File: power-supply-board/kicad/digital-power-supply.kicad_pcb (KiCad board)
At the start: 2 copper layers, 106.5 x 115 mm, 18 parts, among them J1 5V, J2 5V, J3 +12V, J4 +12V, J5 -12V, J6 -12V, SW1 SW

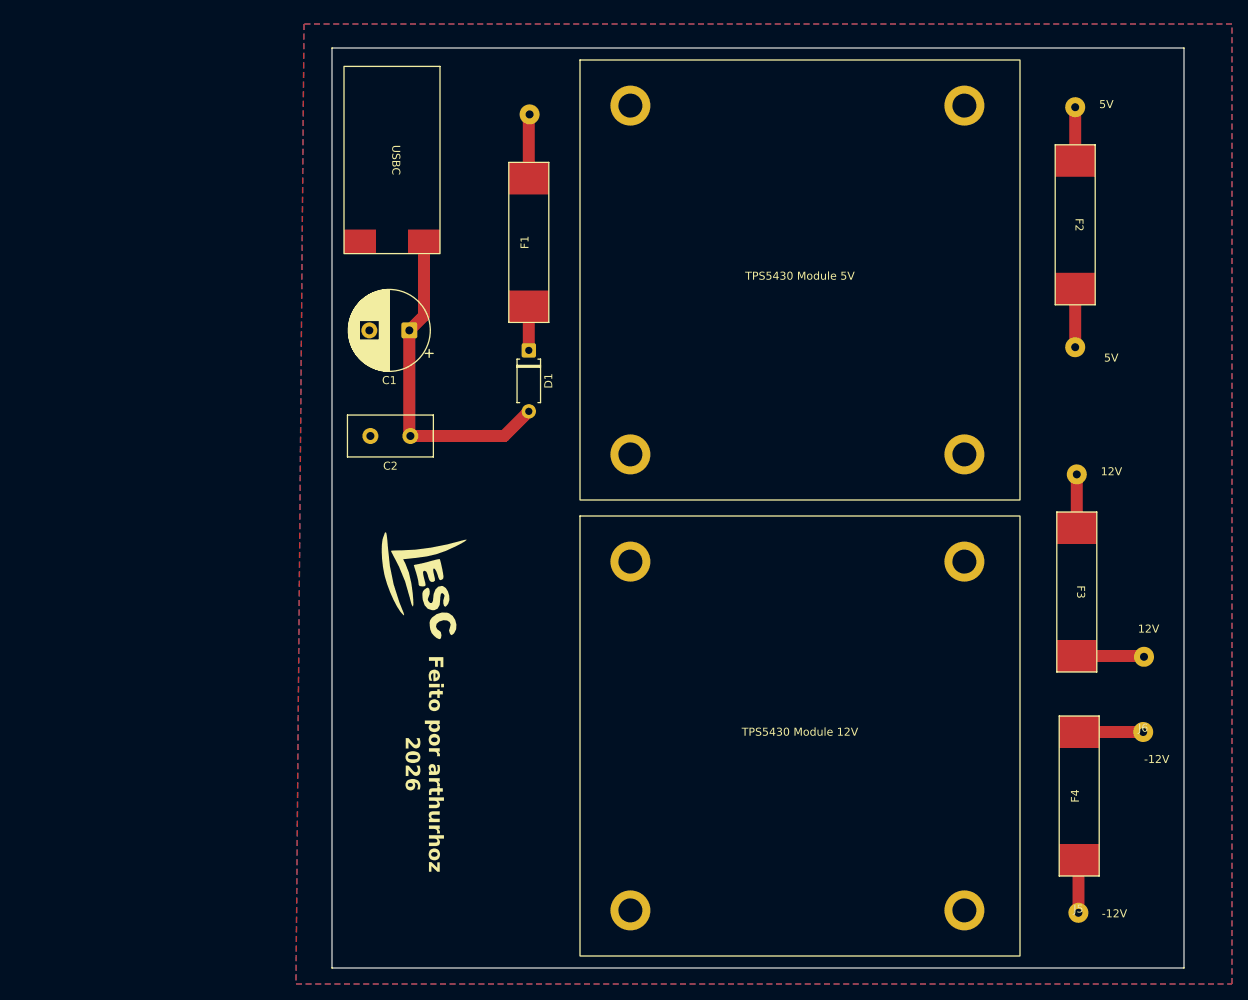
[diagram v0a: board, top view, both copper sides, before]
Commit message: feat: new pcb design with crowbar overvoltage protection
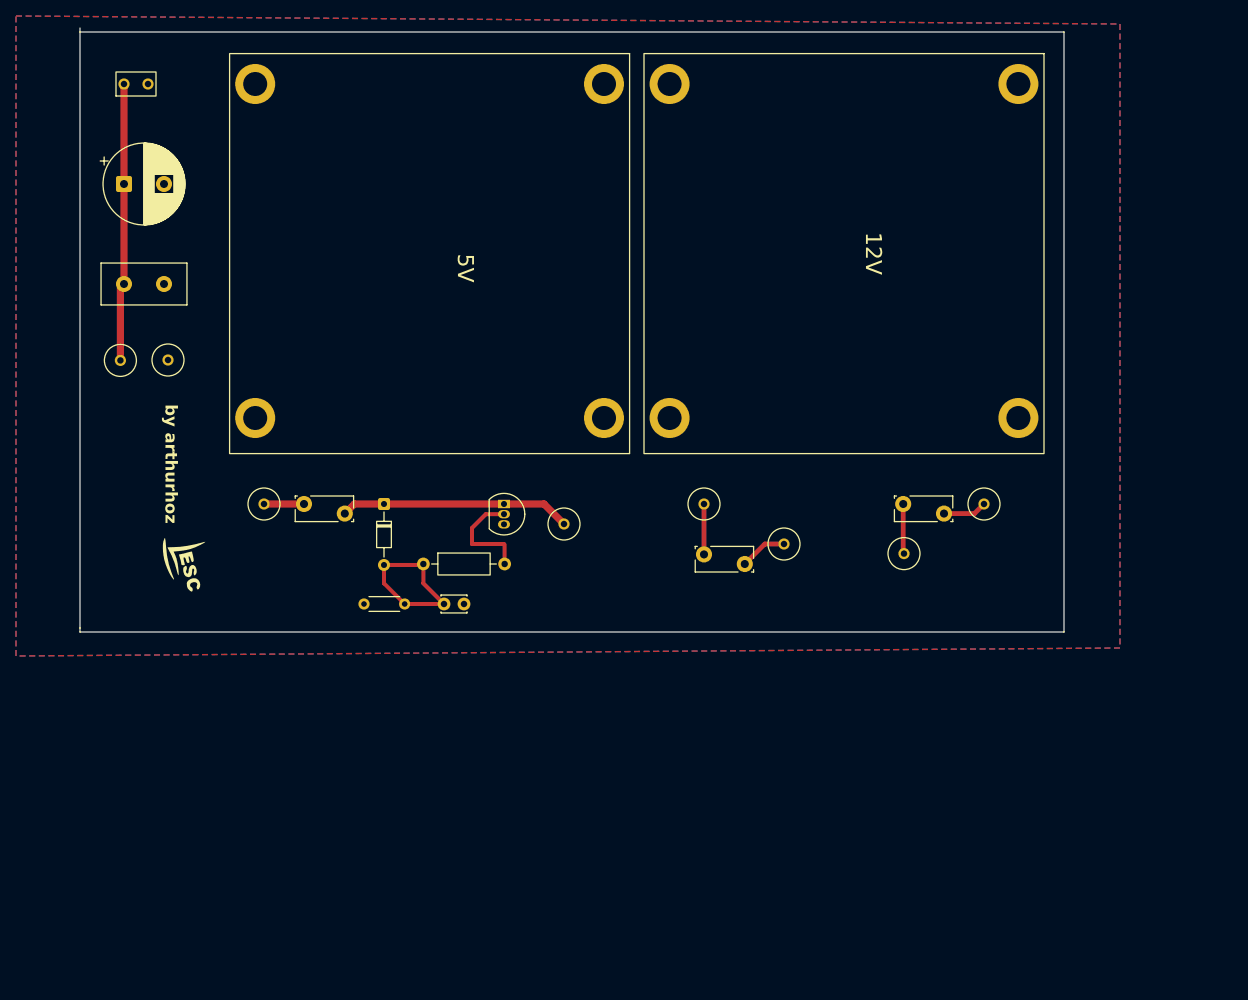
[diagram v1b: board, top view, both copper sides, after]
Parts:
- removed F4: Fuse, footprint:Fuse5x20mm
- removed SW1: SW, footprint:SW
- removed TPS5430 Module 12V: TPS5430 Module 12V, footprint:TPS5430_Module
- removed TPS5430 Module 5V: TPS5430 Module 5V, footprint:TPS5430_Module
- removed USBC: USBC Module, footprint:USBC_Module
- added C4: 1nF, Capacitor_THT:C_Disc_D3.0mm_W2.0mm_P2.50mm, F.Cu at (137.5, 87.5)
- added J7: GND, footprints:Connector, F.Cu at (103.0, 57.0)
- added J8: Conn_01x01_Socket, footprints:Connector, F.Cu at (97.0, 57.0)
- added Q1: BT151-500R, Package_TO_SOT_THT:TO-92_Inline, F.Cu at (145.0, 75.0)
- added R1: 4k7 1/8W, Resistor_THT:R_Axial_DIN0204_L3.6mm_D1.6mm_P5.08mm_Horizontal, F.Cu at (127.5, 87.5)
- added R2: 330 1/4W, Resistor_THT:R_Axial_DIN0207_L6.3mm_D2.5mm_P10.16mm_Horizontal, F.Cu at (134.9, 82.5)
- added U1: USBC Module, footprints:USBC_Module, F.Cu at (99.0, 22.5)
- added U2: TPS5430 Module 5V, footprints:TPS5430_Module, F.Cu at (135.7, 43.7)
- added U3: TPS5430 Module 12V, footprints:TPS5430_Module, F.Cu at (187.5, 43.7)
- D1: value D -> 1N4734A; footprint Diode_THT:D_A-405_P7.62mm_Horizontal -> Diode_THT:D_DO-34_SOD68_P7.62mm_Horizontal
- F1: value Fuse -> RXEF200 2A; footprint footprint:Fuse5x20mm -> Fuse:Fuse_Bourns_MF-RG300
- F2, F3: value Fuse -> RXEF110 1A1; footprint footprint:Fuse5x20mm -> Fuse:Fuse_Bourns_MF-RG300
- J1, J2, J3, J4, J5, J6: footprint footprint:SW -> footprints:Connector
- moved J1 112.9 mm to (115.0, 75.0)
- moved J2 67.6 mm to (152.5, 77.5)
- moved F2 62.1 mm to (170.0, 81.3), turned to 0 degrees
- moved J5 52.4 mm to (205.0, 75.0)
- moved J4 47.2 mm to (180.0, 80.0)
- moved J3 46.7 mm to (170.0, 75.0)
- moved F1 43.1 mm to (120.0, 75.0), turned to 0 degrees
- moved C2 40.5 mm to (97.5, 47.5), turned to 0 degrees
- moved C1 40.1 mm to (97.5, 35.0), turned to 0 degrees
- moved J6 37.3 mm to (195.0, 81.2)
- moved G*** 30.1 mm to (105.0, 82.5)
- moved D1 26.4 mm to (130.0, 75.0)
- moved F3 19.3 mm to (200.0, 76.2), turned to 180 degrees
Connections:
- C1 pad 1: Net-(D1-A) -> /VIN
- C2 pad 1: Net-(D1-A) -> /VIN
- D1 pad 1: Net-(D1-K) -> /5V
- F1 pad 1: Net-(D1-K) -> Net-(J1-Pin_1)
- F1 pad 2: Net-(SW1-B) -> /5V
- F2 pad 1: Net-(J1-Pin_1) -> Net-(J3-Pin_1)
- F2 pad 2: /5V -> /+12V
- F3 pad 1: Net-(J3-Pin_1) -> Net-(J5-Pin_1)
- F3 pad 2: /+12V -> /-12V
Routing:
- net /VIN: track 8.04 -> 34.7 mm
- net /5V: track 7.30 -> 28.9 mm
- net Net-(D1-A): track 41.2 -> 21.9 mm
- net Net-(Q1-G): track 0.00 -> 13.2 mm
- net /-12V: track 14.6 -> 6.24 mm
- net Net-(D1-K): track 5.50 -> 0.00 mm
- net Net-(J5-Pin_1): track 0.00 -> 5.50 mm
- net /+12V: track 8.44 -> 5.94 mm
- net Net-(J1-Pin_1): track 6.70 -> 5.00 mm
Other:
- board size 106.5 x 115 mm -> 123 x 75.5 mm
- board text added: "by arthurhoz"
- board text removed: "-12V"
- board text removed: "Feito por arthurhoz 2026"

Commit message: docs & fix: create schematics and pcb images and remove copper fill in tps modules zones
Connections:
- U1 pad 1: /VIN -> Net-(SW1-B)
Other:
- board size 123 x 75.5 mm -> 125 x 72.5 mm
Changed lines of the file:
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@@
 			(layers "*.Cu" "*.Mask")
 			(remove_unused_layers no)
-			(net "/VIN")
+			(net "Net-(SW1-B)")
 			(pinfunction "VIN_1")
 			(pintype "power_out")
@@
 	)
 	(gr_line
-		(start 92 90.5)
-		(end 92 15.5)
+		(start 88.5 17.5)
+		(end 213.5 17.5)
 		(stroke
 			(width 0.05)
@@
 	)
 	(gr_line
-		(start 92 90.5)
-		(end 92 91)
+		(start 88.5 90)
+		(end 88.5 17.5)
+		(stroke
+			(width 0.05)
+			(type solid)
+		)
+		(layer "Edge.Cuts")
+	)
+	(gr_line
+		(start 213.5 17.5)
+		(end 213.5 90)
 		(stroke
 			(width 0.05)
@@
 	)
 	(gr_line
-		(start 92 91)
-		(end 215 91)
-		(stroke
-			(width 0.05)
-			(type default)
-		)
-		(layer "Edge.Cuts")
-	)
-	(gr_line
-		(start 215 16)
-		(end 91.998984 16)
-		(stroke
-			(width 0.05)
-			(type solid)
-		)
-		(layer "Edge.Cuts")
-	)
-	(gr_line
-		(start 215 16)
-		(end 215 91)
+		(start 213.5 90)
+		(end 88.5 90)
 		(stroke
 			(width 0.05)
@@
 	)
 	(segment
+		(start 97.05 57.05)
+		(end 97.05 47.95)
+		(width 0.9)
+		(layer "F.Cu")
+		(net "/VIN")
+	)
+	(segment
+		(start 97.5 22.5)
+		(end 97.5 35)
+		(width 0.9)
+		(layer "F.Cu")
+		(net "/VIN")
+	)
+	(segment
+		(start 97.5 35)
+		(end 97.5 47.5)
+		(width 0.9)
+		(layer "F.Cu")
+		(net "/VIN")
+	)
+	(segment
+		(start 97.05 47.95)
+		(end 97.5 47.5)
+		(width 0.2)
+		(layer "F.Cu")
+		(net "/VIN")
+	)
+	(segment
+		(start 194.9 81.1)
+		(end 195 81.2)
+		(width 0.2)
+		(layer "F.Cu")
+		(net "/-12V")
+	)
+	(segment
+		(start 194.9 75)
+		(end 194.9 81.1)
+		(width 0.6)
+		(layer "F.Cu")
+		(net "/-12V")
+	)
+	(segment
+		(start 205 75)
+		(end 203.8 76.2)
+		(width 0.6)
+		(layer "F.Cu")
+		(net "Net-(J5-Pin_1)")
+	)
+	(segment
+		(start 203.8 76.2)
+		(end 200 76.2)
+		(width 0.6)
+		(layer "F.Cu")
+		(net "Net-(J5-Pin_1)")
+	)
+	(segment
+		(start 170 75)
+		(end 170 81.3)
+		(width 0.6)
+		(layer "F.Cu")
+		(net "Net-(J3-Pin_1)")
+	)
+	(segment
+		(start 175.1 82.5)
+		(end 177.6 80)
+		(width 0.6)
+		(layer "F.Cu")
+		(net "/+12V")
+	)
+	(segment
+		(start 177.6 80)
+		(end 180 80)
+		(width 0.6)
+		(layer "F.Cu")
+		(net "/+12V")
+	)
+	(segment
+		(start 130 75)
+		(end 145 75)
+		(width 0.9)
+		(layer "F.Cu")
+		(net "/5V")
+	)
+	(segment
+		(start 145 75)
+		(end 150 75)
+		(width 0.9)
+		(layer "F.Cu")
+		(net "/5V")
+	)
+	(segment
+		(start 126.3 75)
+		(end 130 75)
+		(width 0.9)
+		(layer "F.Cu")
+		(net "/5V")
+	)
+	(segment
+		(start 125.1 76.2)
+		(end 126.3 75)
+		(width 0.9)
+		(layer "F.Cu")
+		(net "/5V")
+	)
+	(segment
+		(start 150 75)
+		(end 152.5 77.5)
+		(width 0.9)
+		(layer "F.Cu")
+		(net "/5V")
+	)
+	(segment
+		(start 141 78)
+		(end 142.73 76.27)
+		(width 0.5)
+		(layer "F.Cu")
+		(net "Net-(Q1-G)")
+	)
+	(segment
+		(start 145.08 82.5)
+		(end 145.08 80.08)
+		(width 0.5)
+		(layer "F.Cu")
+		(net "Net-(Q1-G)")
+	)
+	(segment
+		(start 145.08 80.08)
+		(end 145 80)
+		(width 0.2)
+		(layer "F.Cu")
+		(net "Net-(Q1-G)")
+	)
+	(segment
+		(start 141 80)
+		(end 141 78)
+		(width 0.5)
+		(layer "F.Cu")
+		(net "Net-(Q1-G)")
+	)
+	(segment
+		(start 142.73 76.27)
+		(end 145 76.27)
+		(width 0.5)
+		(layer "F.Cu")
+		(net "Net-(Q1-G)")
+	)
+	(segment
+		(start 145 80)
+		(end 141 80)
+		(width 0.5)
+		(layer "F.Cu")
+		(net "Net-(Q1-G)")
+	)
+	(segment
 		(start 115 75)
 		(end 120 75)
@@
 	)
 	(segment
-		(start 130 75)
-		(end 145 75)
-		(width 0.9)
-		(layer "F.Cu")
-		(net "/5V")
-	)
-	(segment
-		(start 145 75)
-		(end 150 75)
-		(width 0.9)
-		(layer "F.Cu")
-		(net "/5V")
-	)
-	(segment
-		(start 126.3 75)
-		(end 130 75)
-		(width 0.9)
-		(layer "F.Cu")
-		(net "/5V")
-	)
-	(segment
-		(start 125.1 76.2)
-		(end 126.3 75)
-		(width 0.9)
-		(layer "F.Cu")
-		(net "/5V")
-	)
-	(segment
-		(start 150 75)
-		(end 152.5 77.5)
-		(width 0.9)
-		(layer "F.Cu")
-		(net "/5V")
-	)
-	(segment
-		(start 205 75)
-		(end 203.8 76.2)
-		(width 0.6)
-		(layer "F.Cu")
-		(net "Net-(J5-Pin_1)")
-	)
-	(segment
-		(start 203.8 76.2)
-		(end 200 76.2)
-		(width 0.6)
-		(layer "F.Cu")
-		(net "Net-(J5-Pin_1)")
-	)
-	(segment
 		(start 132.58 87.5)
 		(end 137.5 87.5)
@@
 		(net "Net-(D1-A)")
 	)
-	(segment
-		(start 194.9 81.1)
-		(end 195 81.2)
-		(width 0.2)
-		(layer "F.Cu")
-		(net "/-12V")
-	)
-	(segment
-		(start 194.9 75)
-		(end 194.9 81.1)
-		(width 0.6)
-		(layer "F.Cu")
-		(net "/-12V")
-	)
-	(segment
-		(start 97.05 57.05)
-		(end 97.05 47.95)
-		(width 0.9)
-		(layer "F.Cu")
-		(net "/VIN")
-	)
-	(segment
-		(start 97.5 22.5)
-		(end 97.5 35)
-		(width 0.9)
-		(layer "F.Cu")
-		(net "/VIN")
-	)
-	(segment
-		(start 97.5 35)
-		(end 97.5 47.5)
-		(width 0.9)
-		(layer "F.Cu")
-		(net "/VIN")
-	)
-	(segment
-		(start 97.05 47.95)
-		(end 97.5 47.5)
-		(width 0.2)
-		(layer "F.Cu")
-		(net "/VIN")
-	)
-	(segment
-		(start 175.1 82.5)
-		(end 177.6 80)
-		(width 0.6)
-		(layer "F.Cu")
-		(net "/+12V")
-	)
-	(segment
-		(start 177.6 80)
-		(end 180 80)
-		(width 0.6)
-		(layer "F.Cu")
-		(net "/+12V")
-	)
-	(segment
-		(start 170 75)
-		(end 170 81.3)
-		(width 0.6)
-		(layer "F.Cu")
-		(net "Net-(J3-Pin_1)")
-	)
-	(segment
-		(start 141 78)
-		(end 142.73 76.27)
-		(width 0.5)
-		(layer "F.Cu")
-		(net "Net-(Q1-G)")
-	)
-	(segment
-		(start 145.08 82.5)
-		(end 145.08 80.08)
-		(width 0.5)
-		(layer "F.Cu")
-		(net "Net-(Q1-G)")
-	)
-	(segment
-		(start 145.08 80.08)
-		(end 145 80)
-		(width 0.2)
-		(layer "F.Cu")
-		(net "Net-(Q1-G)")
-	)
-	(segment
-		(start 141 80)
-		(end 141 78)
-		(width 0.5)
-		(layer "F.Cu")
-		(net "Net-(Q1-G)")
-	)
-	(segment
-		(start 142.73 76.27)
-		(end 145 76.27)
-		(width 0.5)
-		(layer "F.Cu")
-		(net "Net-(Q1-G)")
-	)
-	(segment
-		(start 145 80)
-		(end 141 80)
-		(width 0.5)
-		(layer "F.Cu")
-		(net "Net-(Q1-G)")
+	(zone
+		(layers "F.Cu" "B.Cu")
+		(hatch edge 0.5)
+		(connect_pads
+			(clearance 0)
+		)
+		(min_thickness 0.25)
+		(keepout
+			(tracks not_allowed)
+			(vias not_allowed)
+			(pads not_allowed)
+			(copperpour not_allowed)
+			(footprints allowed)
+		)
+		(placement
+			(enabled no)
+			(sheetname "")
+		)
+		(fill
+			(thermal_gap 0.5)
+			(thermal_bridge_width 0.5)
+			(island_removal_mode 0)
+		)
+		(polygon
+			(pts
+				(xy 110.72 18.72) (xy 160.69 18.71) (xy 160.7 68.69) (xy 110.7 68.69)
+			)
+		)
+	)
+	(zone
+		(layers "F.Cu" "B.Cu")
+		(hatch edge 0.5)
+		(connect_pads
+			(clearance 0)
+		)
+		(min_thickness 0.25)
+		(keepout
+			(tracks not_allowed)
+			(vias not_allowed)
+			(pads not_allowed)
+			(copperpour not_allowed)
+			(footprints allowed)
+		)
+		(placement
+			(enabled no)
+			(sheetname "")
+		)
+		(fill
+			(thermal_gap 0.5)
+			(thermal_bridge_width 0.5)
+			(island_removal_mode 0)
+		)
+		(polygon
+			(pts
+				(xy 162.5 18.71) (xy 212.5 18.71) (xy 212.49 68.68) (xy 162.51 68.69)
+			)
+		)
 	)
 	(zone
 		(net "GND")
 		(layers "F.Cu" "B.Cu")
-		(name "Ground Plane")
 		(hatch edge 0.5)
 		(connect_pads
@@
 		(polygon
 			(pts
-				(xy 84 94) (xy 84 14) (xy 222 15) (xy 222 93)
-			)
-		)
+				(xy 217 93) (xy 216.5 14) (xy 84.5 14.5) (xy 84.5 93.5)
+			)
+		)

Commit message: feat: increase tracks width and add zone rules
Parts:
- added J9: 5V, footprints:Connector, F.Cu at (125.1, 81.9)
- J7: footprint footprints:Connector -> footprints:ConnectorGND
- U2: moved to B.Cu
- moved G*** 4.11 mm to (101.2, 84.1)
- moved J7 0.97 mm to (103.9, 57.3)
- moved J8 0.47 mm to (97.4, 57.3)
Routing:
- net /5V: track 28.9 -> 34.6 mm
- net /VIN: track 34.7 -> 36.7 mm
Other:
- board text added: "+12V"
- board text added: "+5V"
- board text added: "-12V"
- board text added: "GND"
- board text added: "VIN"
